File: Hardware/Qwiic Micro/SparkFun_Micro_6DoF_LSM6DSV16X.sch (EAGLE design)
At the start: 29 parts, among them J1 Qwiic Right Angle, U2 LSM6DSV16X

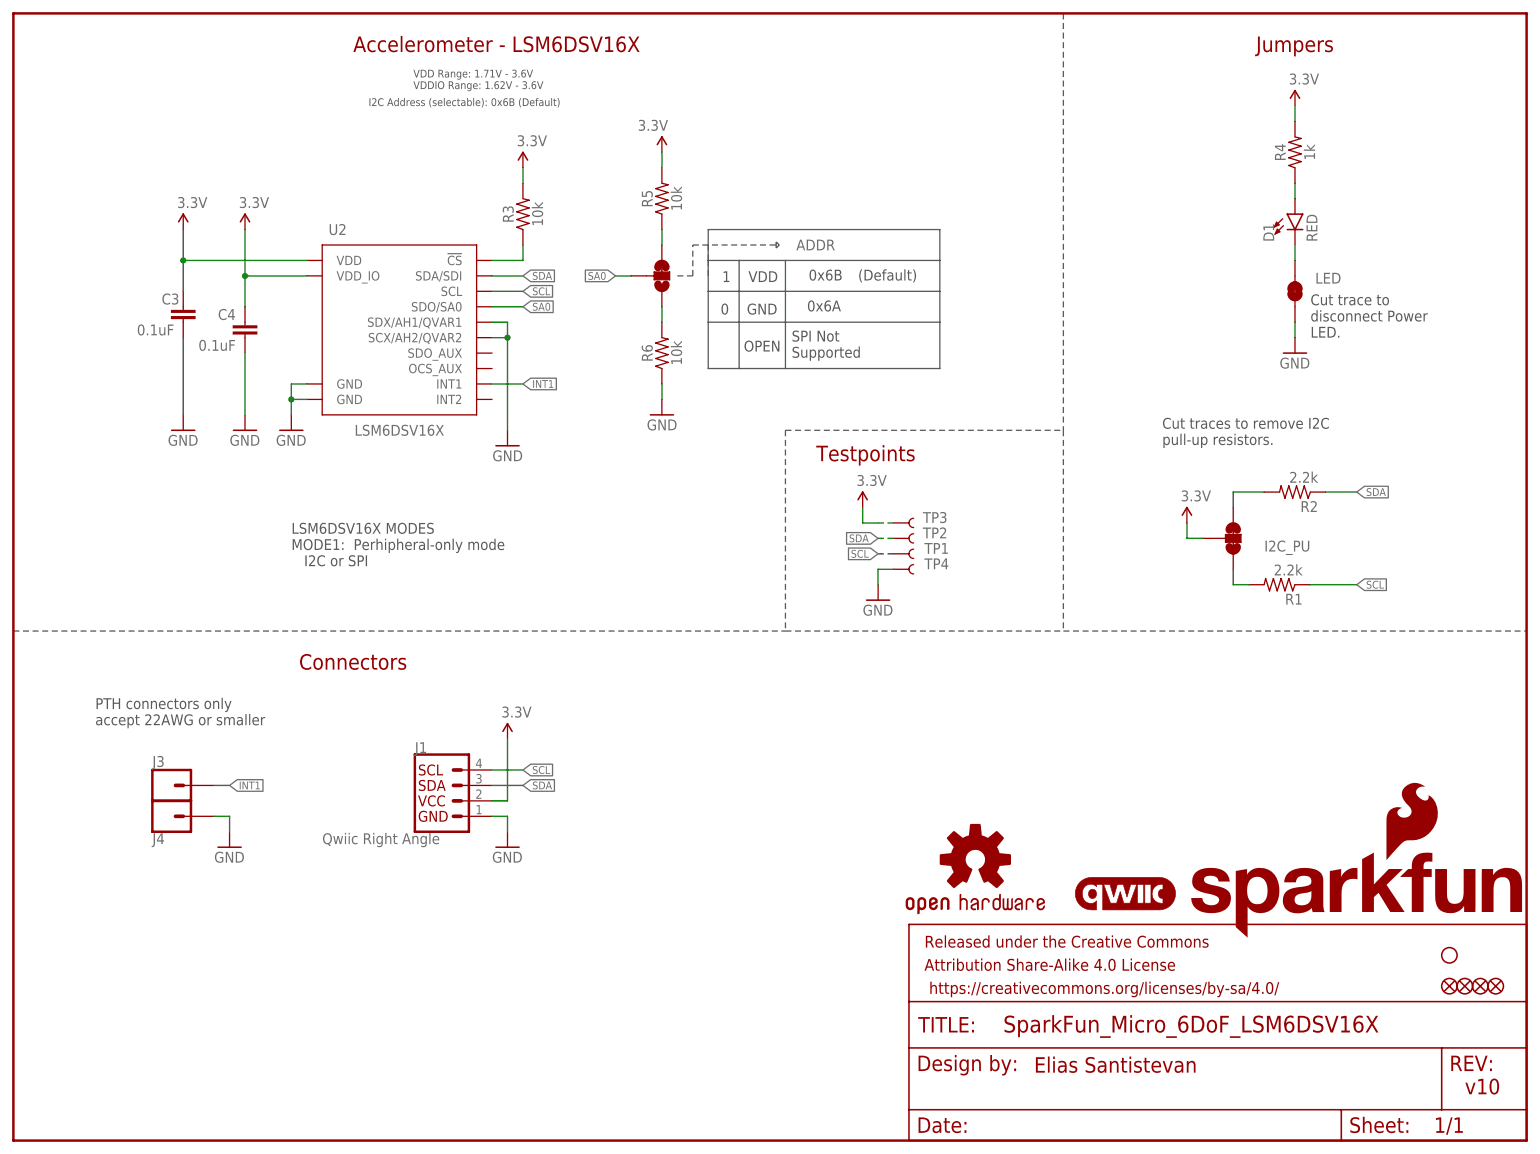
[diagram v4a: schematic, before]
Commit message: Increases pad size, decreases paste size on footprint
* Also adds trestrict between ground pads to the footprint itself
* Fixes gyro silk on bottom
* Swaps PICO and CS on 1x1 header
* Improves ground pour
* Adds more notes to the filter section
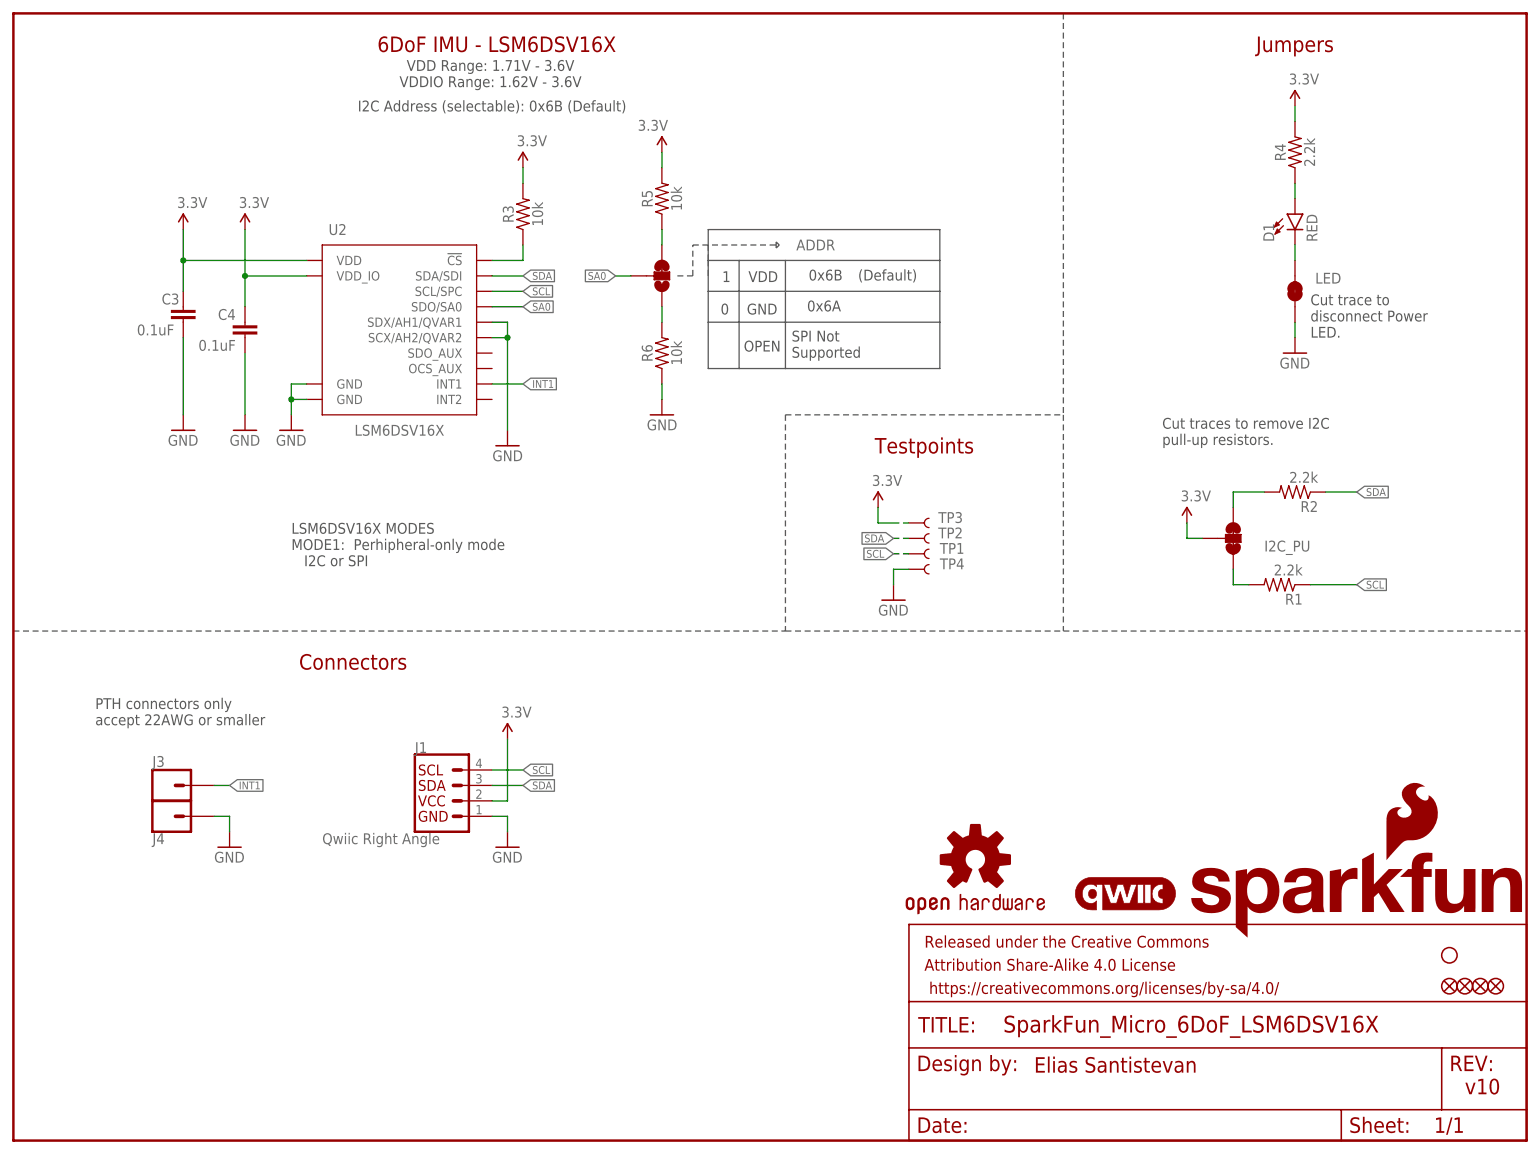
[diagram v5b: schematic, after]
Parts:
- R4: value 1k -> 2.2k; device SparkFun-Resistors:1KOHM-0402T-1/16W-1% -> SparkFun-Resistors:2.2KOHM-0402T-1/16W-1%
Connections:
- net SCL: now also U2.SCL/SPC; no longer U2.SCL
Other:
- note added: "6DoF IMU - LSM6DSV16X"
- note removed: "Accelerometer - LSM6DSV16X"
- moved on the sheet: TP1, TP2, TP3, TP4
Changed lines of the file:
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@@
 <part name="FD2" library="SparkFun-Aesthetics" deviceset="FIDUCIAL" device="UFIDUCIAL"/>
 <part name="D1" library="SparkFun-LED" deviceset="LED-RED" device="_0402" value="RED"/>
-<part name="R4" library="SparkFun-Resistors" deviceset="1KOHM" device="-0402T-1/16W-1%" value="1k"/>
+<part name="R4" library="SparkFun-Resistors" deviceset="2.2KOHM" device="-0402T-1/16W-1%" value="2.2k"/>
 <part name="LED" library="SparkFun-Jumpers" deviceset="JUMPER-SMT_2_NC_TRACE" device="_SILK" package3d_urn="urn:adsk.eagle:package:39281/1"/>
 <part name="SUPPLY3" library="SparkFun-PowerSymbols" deviceset="3.3V" device=""/>
@@
 <sheet>
 <plain>
-<text x="79.502" y="180.34" size="2.54" layer="94" font="vector" align="center">Accelerometer - LSM6DSV16X</text>
+<text x="79.502" y="180.34" size="2.54" layer="94" font="vector" align="center">6DoF IMU - LSM6DSV16X</text>
 <text x="188.976" y="118.872" size="1.778" layer="97" font="vector" align="top-left">Cut traces to remove I2C
 pull-up resistors.</text>
@@
 <wire x1="0" y1="83.82" x2="127" y2="83.82" width="0.2032" layer="97" style="longdash"/>
 <wire x1="172.72" y1="83.82" x2="248.92" y2="83.82" width="0.2032" layer="97" style="longdash"/>
-<wire x1="172.72" y1="185.42" x2="172.72" y2="116.84" width="0.2032" layer="97" style="longdash"/>
-<text x="65.786" y="172.974" size="1.27" layer="97" font="vector">VDD Range: 1.71V - 3.6V
+<wire x1="172.72" y1="185.42" x2="172.72" y2="119.38" width="0.2032" layer="97" style="longdash"/>
+<text x="78.486" y="175.514" size="1.778" layer="97" font="vector" align="center">VDD Range: 1.71V - 3.6V
 VDDIO Range: 1.62V - 3.6V</text>
 <text x="238.76" y="7.62" size="2.54" layer="94" font="vector">v10</text>
@@
 LED.</text>
 <text x="55.88" y="78.74" size="2.54" layer="94" font="vector" align="center">Connectors</text>
-<wire x1="172.72" y1="116.84" x2="172.72" y2="83.82" width="0.2032" layer="97" style="longdash"/>
+<wire x1="172.72" y1="119.38" x2="172.72" y2="83.82" width="0.2032" layer="97" style="longdash"/>
 <wire x1="119.38" y1="144.78" x2="119.38" y2="139.7" width="0.2032" layer="97"/>
 <wire x1="119.38" y1="139.7" x2="119.38" y2="134.62" width="0.2032" layer="97"/>
@@
 <wire x1="125.476" y1="147.828" x2="125.476" y2="146.812" width="0.2032" layer="97" style="dashdot"/>
 <wire x1="125.476" y1="146.812" x2="125.984" y2="147.32" width="0.2032" layer="97" style="dashdot"/>
-<wire x1="127" y1="116.84" x2="172.72" y2="116.84" width="0.2032" layer="97" style="longdash"/>
-<text x="132.08" y="111.76" size="2.54" layer="94" font="vector">Testpoints</text>
+<wire x1="127" y1="119.38" x2="172.72" y2="119.38" width="0.2032" layer="97" style="longdash"/>
+<text x="149.86" y="114.3" size="2.54" layer="94" font="vector" align="center">Testpoints</text>
 <text x="138.938" y="141.478" size="1.778" layer="97" font="vector">(Default)</text>
-<wire x1="127" y1="116.84" x2="127" y2="83.82" width="0.2032" layer="97" style="longdash"/>
+<wire x1="127" y1="119.38" x2="127" y2="83.82" width="0.2032" layer="97" style="longdash"/>
 <wire x1="127" y1="83.82" x2="172.72" y2="83.82" width="0.2032" layer="97" style="longdash"/>
-<text x="58.42" y="170.18" size="1.27" layer="97" font="vector">I2C Address (selectable): 0x6B (Default)</text>
+<text x="78.74" y="170.18" size="1.778" layer="97" font="vector" align="center">I2C Address (selectable): 0x6B (Default)</text>
 <text x="13.462" y="68.326" size="1.778" layer="97" font="vector">PTH connectors only
 accept 22AWG or smaller</text>
@@
 <instance part="LOGO1" gate="G$1" x="182.88" y="40.64" smashed="yes"/>
 <instance part="LOGO3" gate="G$1" x="193.04" y="33.02" smashed="yes"/>
-<instance part="TP1" gate="G$1" x="144.78" y="96.52" smashed="yes">
-<attribute name="NAME" x="149.86" y="96.52" size="1.778" layer="95" font="vector"/>
-</instance>
-<instance part="TP2" gate="G$1" x="144.78" y="99.06" smashed="yes">
-<attribute name="NAME" x="149.606" y="99.06" size="1.778" layer="95" font="vector"/>
-</instance>
-<instance part="TP3" gate="G$1" x="144.78" y="101.6" smashed="yes">
-<attribute name="NAME" x="149.606" y="101.6" size="1.778" layer="95" font="vector"/>
-</instance>
-<instance part="SUPPLY6" gate="G$1" x="139.7" y="104.14" smashed="yes">
-<attribute name="VALUE" x="138.684" y="107.696" size="1.778" layer="96" font="vector"/>
+<instance part="TP1" gate="G$1" x="147.32" y="96.52" smashed="yes">
+<attribute name="NAME" x="152.4" y="96.52" size="1.778" layer="95" font="vector"/>
+</instance>
+<instance part="TP2" gate="G$1" x="147.32" y="99.06" smashed="yes">
+<attribute name="NAME" x="152.146" y="99.06" size="1.778" layer="95" font="vector"/>
+</instance>
+<instance part="TP3" gate="G$1" x="147.32" y="101.6" smashed="yes">
+<attribute name="NAME" x="152.146" y="101.6" size="1.778" layer="95" font="vector"/>
+</instance>
+<instance part="SUPPLY6" gate="G$1" x="142.24" y="104.14" smashed="yes">
+<attribute name="VALUE" x="141.224" y="107.696" size="1.778" layer="96" font="vector"/>
 </instance>
 <instance part="J3" gate="G$1" x="25.4" y="58.42" smashed="yes">
@@
 <attribute name="VALUE" x="33.02" y="45.72" size="1.778" layer="96" font="vector"/>
 </instance>
-<instance part="TP4" gate="G$1" x="144.78" y="93.98" smashed="yes">
-<attribute name="NAME" x="149.86" y="93.98" size="1.778" layer="95" font="vector"/>
-</instance>
-<instance part="GND1" gate="1" x="142.24" y="88.9" smashed="yes">
-<attribute name="VALUE" x="139.7" y="86.36" size="1.778" layer="96" font="vector"/>
+<instance part="TP4" gate="G$1" x="147.32" y="93.98" smashed="yes">
+<attribute name="NAME" x="152.4" y="93.98" size="1.778" layer="95" font="vector"/>
+</instance>
+<instance part="GND1" gate="1" x="144.78" y="88.9" smashed="yes">
+<attribute name="VALUE" x="142.24" y="86.36" size="1.778" layer="96" font="vector"/>
 </instance>
 <instance part="R3" gate="G$1" x="83.82" y="152.4" smashed="yes" rot="R90">
@@
 <segment>
 <pinref part="TP4" gate="G$1" pin="1"/>
-<wire x1="144.78" y1="93.98" x2="142.24" y2="93.98" width="0.1524" layer="91"/>
-<wire x1="142.24" y1="93.98" x2="142.24" y2="91.44" width="0.1524" layer="91"/>
+<wire x1="147.32" y1="93.98" x2="144.78" y2="93.98" width="0.1524" layer="91"/>
+<wire x1="144.78" y1="93.98" x2="144.78" y2="91.44" width="0.1524" layer="91"/>
 <pinref part="GND1" gate="1" pin="GND"/>
 </segment>
@@
 <wire x1="78.74" y1="139.7" x2="83.82" y2="139.7" width="0.1524" layer="91"/>
 <label x="83.82" y="139.7" size="1.27" layer="95" font="vector" xref="yes"/>
-<pinref part="U2" gate="G$1" pin="SCL"/>
+<pinref part="U2" gate="G$1" pin="SCL/SPC"/>
 </segment>
 <segment>
@@
 <segment>
 <pinref part="TP1" gate="G$1" pin="1"/>
-<wire x1="144.78" y1="96.52" x2="142.24" y2="96.52" width="0.1524" layer="91" style="dashdot"/>
-<label x="142.24" y="96.52" size="1.27" layer="95" font="vector" rot="R180" xref="yes"/>
+<wire x1="147.32" y1="96.52" x2="144.78" y2="96.52" width="0.1524" layer="91" style="dashdot"/>
+<label x="144.78" y="96.52" size="1.27" layer="95" font="vector" rot="R180" xref="yes"/>
 </segment>
 </net>
@@
 <segment>
 <pinref part="TP2" gate="G$1" pin="1"/>
-<wire x1="144.78" y1="99.06" x2="142.24" y2="99.06" width="0.1524" layer="91" style="dashdot"/>
-<label x="142.24" y="99.06" size="1.27" layer="95" font="vector" rot="R180" xref="yes"/>
+<wire x1="147.32" y1="99.06" x2="144.78" y2="99.06" width="0.1524" layer="91" style="dashdot"/>
+<label x="144.78" y="99.06" size="1.27" layer="95" font="vector" rot="R180" xref="yes"/>
 </segment>
 </net>
@@
 <segment>
 <pinref part="TP3" gate="G$1" pin="1"/>
-<wire x1="144.78" y1="101.6" x2="142.24" y2="101.6" width="0.1524" layer="91" style="dashdot"/>
-<wire x1="142.24" y1="101.6" x2="139.7" y2="101.6" width="0.1524" layer="91"/>
-<wire x1="139.7" y1="101.6" x2="139.7" y2="104.14" width="0.1524" layer="91"/>
+<wire x1="147.32" y1="101.6" x2="144.78" y2="101.6" width="0.1524" layer="91" style="dashdot"/>
+<wire x1="144.78" y1="101.6" x2="142.24" y2="101.6" width="0.1524" layer="91"/>
+<wire x1="142.24" y1="101.6" x2="142.24" y2="104.14" width="0.1524" layer="91"/>
 <pinref part="SUPPLY6" gate="G$1" pin="3.3V"/>
 </segment>
